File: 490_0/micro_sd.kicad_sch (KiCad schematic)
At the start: 5 parts, among them J26 Micro_SD_Card, U27 RT9742GGJ5

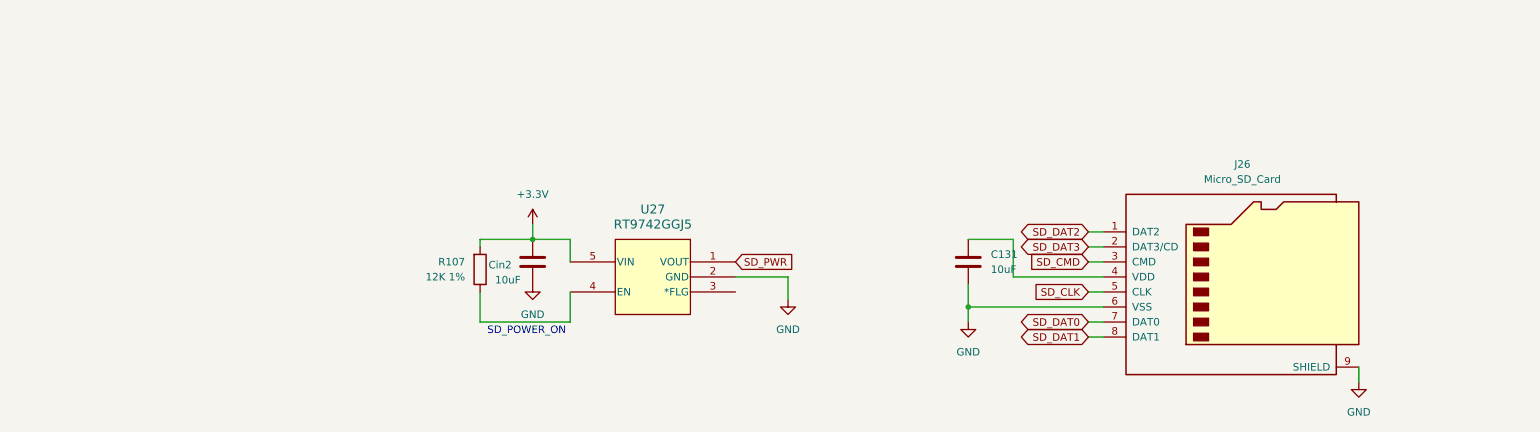
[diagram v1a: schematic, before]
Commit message: Changed some local labels to the right format
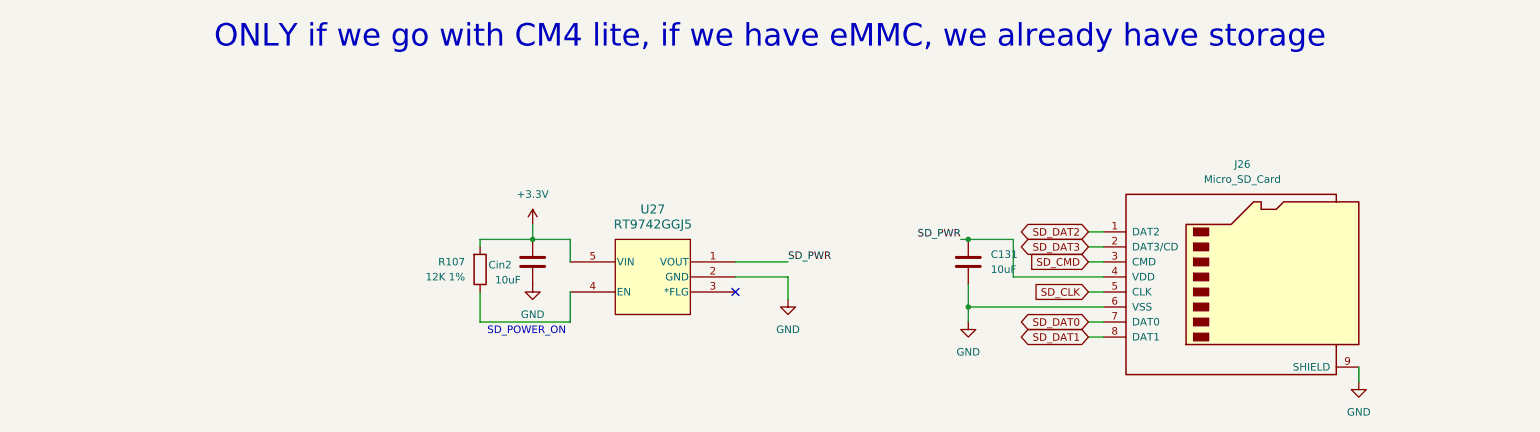
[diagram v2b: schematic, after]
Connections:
- net SD_PWR: now also C131.1, J26.4 (VDD)
- no-connect marks 0 -> 1
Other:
- note added: "ONLY if we go with CM4 lite, if we have eMMC, we already have storage"
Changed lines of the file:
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@@
+		)
+	)
+	(text "ONLY if we go with CM4 lite, if we have eMMC, we already have storage\n"
+		(exclude_from_sim no)
+		(at 123.952 50.8 0)
+		(effects
+			(font
+				(size 3.81 3.81)
+			)
 		)
 	)
@@
 	)
 	(junction
+		(at 157.48 85.09)
+		(diameter 0)
+		(color 0 0 0 0)
+	)
+	(junction
 		(at 157.48 96.52)
 		(diameter 0)
 		(color 0 0 0 0)
 	)
+	(no_connect
+		(at 118.11 93.98)
+	)
 	(wire
 		(pts
@@
 	(wire
 		(pts
+			(xy 156.21 85.09) (xy 157.48 85.09)
+		)
+		(stroke
+			(width 0)
+			(type default)
+		)
+	)
+	(wire
+		(pts
 			(xy 177.8 83.82) (xy 180.34 83.82)
 		)
@@
 	(wire
 		(pts
-			(xy 165.1 85.09) (xy 157.48 85.09)
-		)
-		(stroke
-			(width 0)
-			(type default)
-		)
-	)
-	(wire
-		(pts
 			(xy 157.48 92.71) (xy 157.48 96.52)
 		)
@@
 	(wire
 		(pts
+			(xy 157.48 85.09) (xy 165.1 85.09)
+		)
+		(stroke
+			(width 0)
+			(type default)
+		)
+	)
+	(wire
+		(pts
+			(xy 127 88.9) (xy 118.11 88.9)
+		)
+		(stroke
+			(width 0)
+			(type default)
+		)
+	)
+	(wire
+		(pts
 			(xy 177.8 88.9) (xy 180.34 88.9)
 		)
@@
 			(width 0)
 			(type default)
+		)
+	)
+	(label "SD_PWR"
+		(at 127 88.9 0)
+		(effects
+			(font
+				(size 1.27 1.27)
+			)
+			(justify left bottom)
+		)
+	)
+	(label "SD_PWR"
+		(at 156.21 85.09 180)
+		(effects
+			(font
+				(size 1.27 1.27)
+			)
+			(justify right bottom)
 		)
 	)
@@
 			(effects
 				(font
-					(size 1.27 1.27)
-				)
-				(hide yes)
-			)
-		)
-	)
-	(global_label "SD_PWR"
-		(shape input)
-		(at 118.11 88.9 0)
-		(effects
-			(font
-				(size 1.27 1.27)
-			)
-			(justify left)
-		)
-		(property "Intersheetrefs" "${INTERSHEET_REFS}"
-			(at 118.11 88.9 0)
-			(effects
-				(font
